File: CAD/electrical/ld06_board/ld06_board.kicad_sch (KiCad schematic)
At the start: 9 parts, among them J1 RS485, J2 LED Strip, J3 Conn_01x04_Pin, J4 I2C, U1 MAX485E, U2 SeeeduinoXIAO

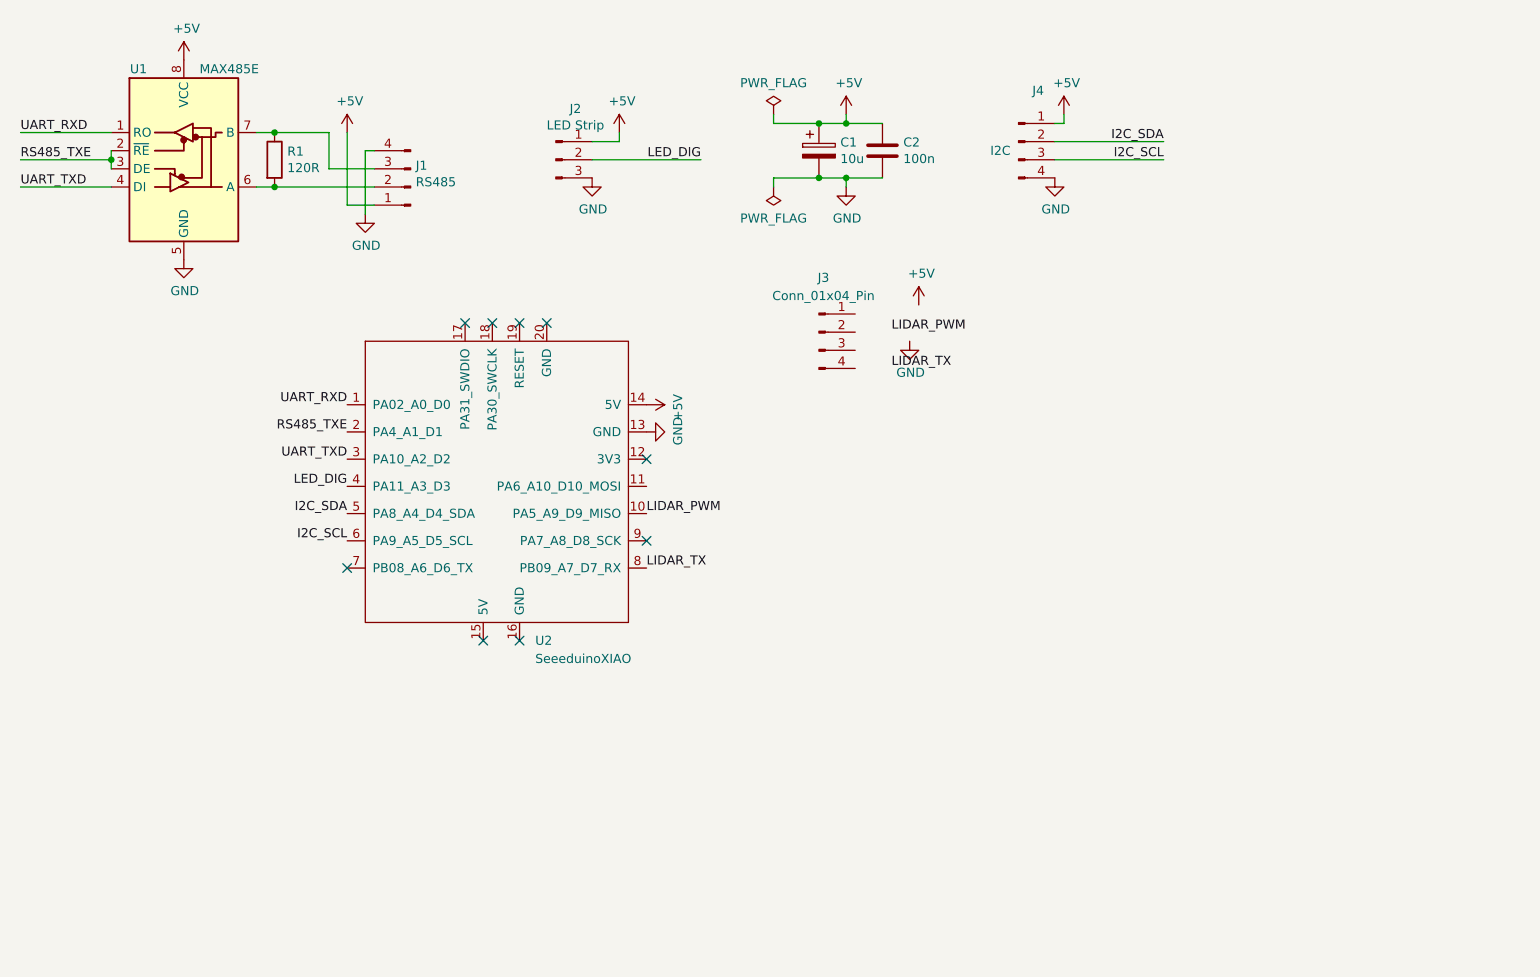
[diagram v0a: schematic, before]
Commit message: sync LD06 board
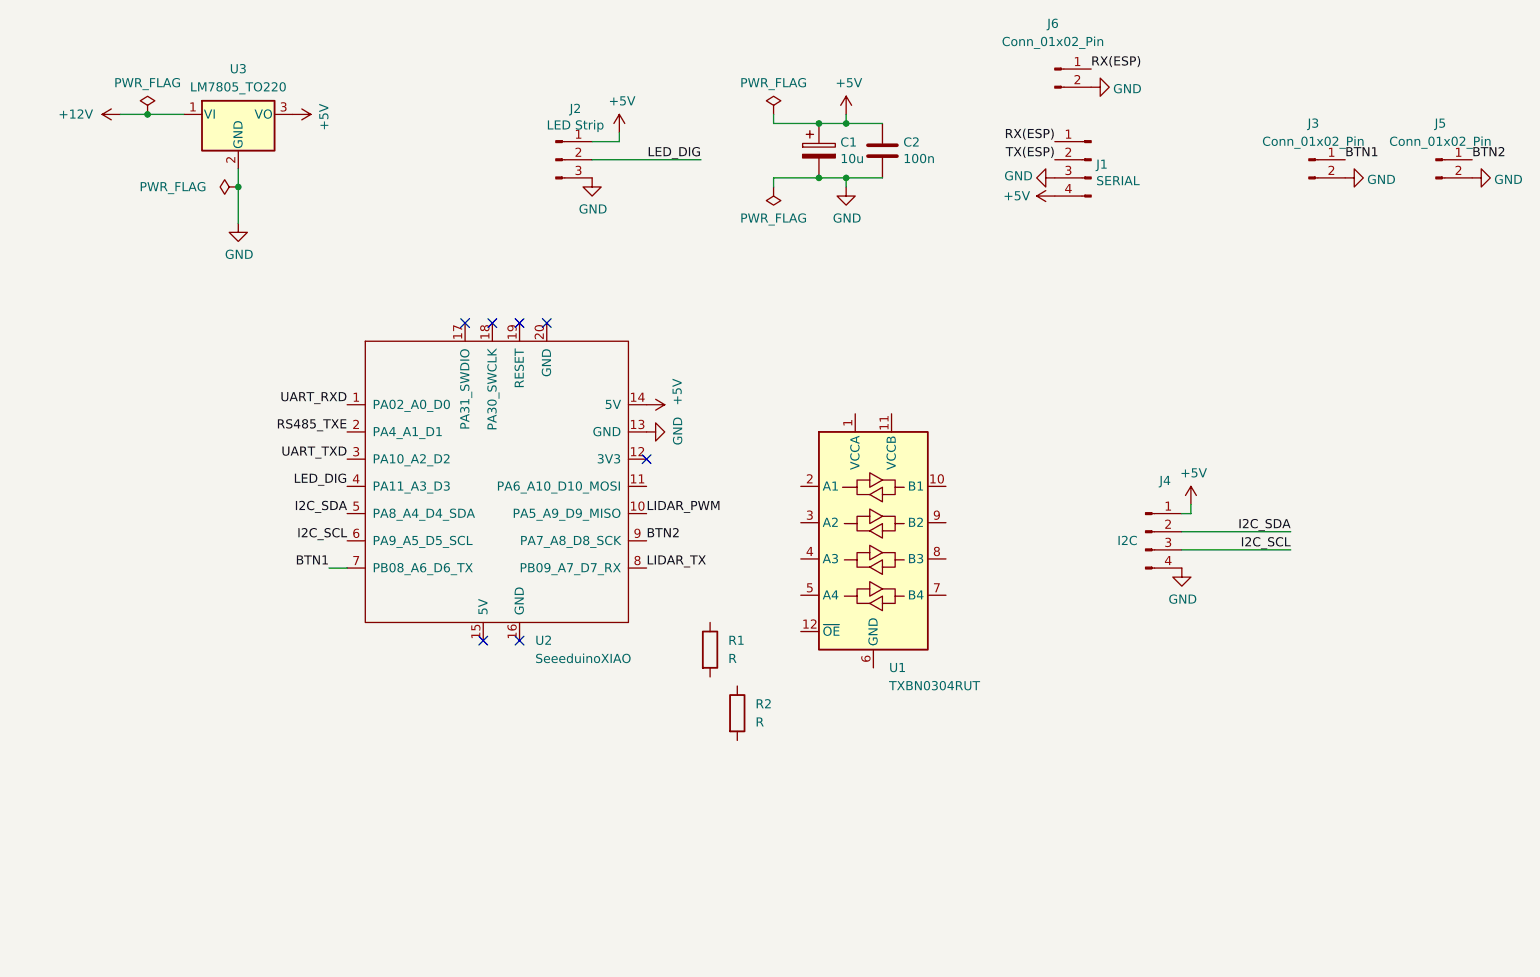
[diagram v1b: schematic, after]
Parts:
- removed J3: Conn_01x04_Pin, Connector_Molex:Molex_KK-254_AE-6410-04A_1x04_P2.54mm_Vertical, symbol Connector:Conn_01x04_Pin
- removed U1: MAX485E, Package_SO:SOIC-8_3.9x4.9mm_P1.27mm, symbol Interface_UART:MAX485E
- added J3, J5, J6: Conn_01x02_Pin, Connector_Molex:Molex_KK-254_AE-6410-02A_1x02_P2.54mm_Vertical, symbol Connector:Conn_01x02_Pin
- added R2: R, Resistor_THT:R_Axial_DIN0309_L9.0mm_D3.2mm_P12.70mm_Horizontal, symbol Device:R
- added U1: TXBN0304RUT, Package_DIP:DIP-12_W10.16mm, symbol Logic_LevelTranslator:TXBN0304RUT
- added U3: LM7805_TO220, Package_TO_SOT_THT:TO-220-3_Vertical, symbol Regulator_Linear:LM7805_TO220
- J1: value RS485 -> SERIAL
- R1: value 120R -> R; footprint Resistor_SMD:R_0603_1608Metric -> Resistor_THT:R_Axial_DIN0309_L9.0mm_D3.2mm_P12.70mm_Horizontal
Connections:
- net +5V: now also J1.4 (Pin_4), U3.3 (VO); no longer J1.1 (Pin_1)
- net GND: now also J1.3 (Pin_3), J3.2 (Pin_2), J5.2 (Pin_2), J6.2 (Pin_2), U3.2 (GND); no longer J1.4 (Pin_4)
- net at R1.2: no longer J1.2 (Pin_2)
- net at R1.1: no longer J1.3 (Pin_3)
- net BTN1: now reaches U2.7 (PB08_A6_D6_TX)
- net BTN1: now also J3.1 (Pin_1)
- net BTN2: now reaches U2.9 (PA7_A8_D8_SCK)
- net BTN2: now also J5.1 (Pin_1)
- new net +12V: U3.1 (VI)
- new net RX(ESP): J1.1 (Pin_1), J6.1 (Pin_1)
- new net TX(ESP): J1.2 (Pin_2)
- no-connect marks 9 -> 7
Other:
- moved on the sheet: J4

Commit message: update PCB
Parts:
- added J7: I2C, Connector_Molex:Molex_KK-254_AE-6410-04A_1x04_P2.54mm_Vertical, symbol Connector:Conn_01x04_Male
- added J9: Battery in, Connector_BarrelJack:BarrelJack_Horizontal, symbol main_board-rescue:Conn_01x02_Male-Connector
- C2: footprint Capacitor_SMD:C_0603_1608Metric -> Resistor_THT:R_Axial_DIN0204_L3.6mm_D1.6mm_P5.08mm_Vertical
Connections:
- net +12V: now also J9.1 (Pin_1)
- net +5V: now also J7.1 (Pin_1)
- net GND: now also J7.4 (Pin_4), J9.2 (Pin_2)
- net I2C_SCL: now also J7.3 (Pin_3)
- net I2C_SDA: now also J7.2 (Pin_2)

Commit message: update
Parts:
- removed U2: SeeeduinoXIAO, Seeeduino XIAO KICAD:XIAO-ESP32-C3-DIP, symbol Seeeduino XIAO:SeeeduinoXIAO
- added U2: ESP32-C3_SUPERMINI_TH, ESP32-C3_SUPERMINI_TH:MODULE_ESP32-C3_SUPERMINI, symbol ESP32-C3_SUPERMINI_TH:ESP32-C3_SUPERMINI_TH
- U1: footprint Package_DIP:DIP-12_W10.16mm -> (none)
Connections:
- net +5V: now also U1.1 (VCCA), U2.5V
- net BTN1: now also U2.5 (GPIO5)
- net BTN2: now also U2.7 (GPIO7)
- net GND: now also U1.12 (~{OE}), U1.6 (GND), U2.G (GND)
- net I2C_SCL: now also U1.2 (A1)
- net I2C_SDA: now also U1.3 (A2)
- net LED_DIG: now also U2.1 (GPIO1)
- net RX(ESP): now also U2.20 (GPIO20)
- net TX(ESP): now also U2.21 (GPIO21)
- net 3V3_SCL: now reaches R2.1
- net 3V3_SCL: now also U1.10 (B1), U2.4 (GPIO4)
- net +3V3: now reaches R2.2
- net +3V3: now also R1.2, U1.11 (VCCB), U2.3.3 (3V3)
- net 3V3_SDA: now reaches R1.1
- net 3V3_SDA: now also U1.9 (B2), U2.3 (GPIO3)
- no-connect marks 7 -> 10
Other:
- moved on the sheet: U1

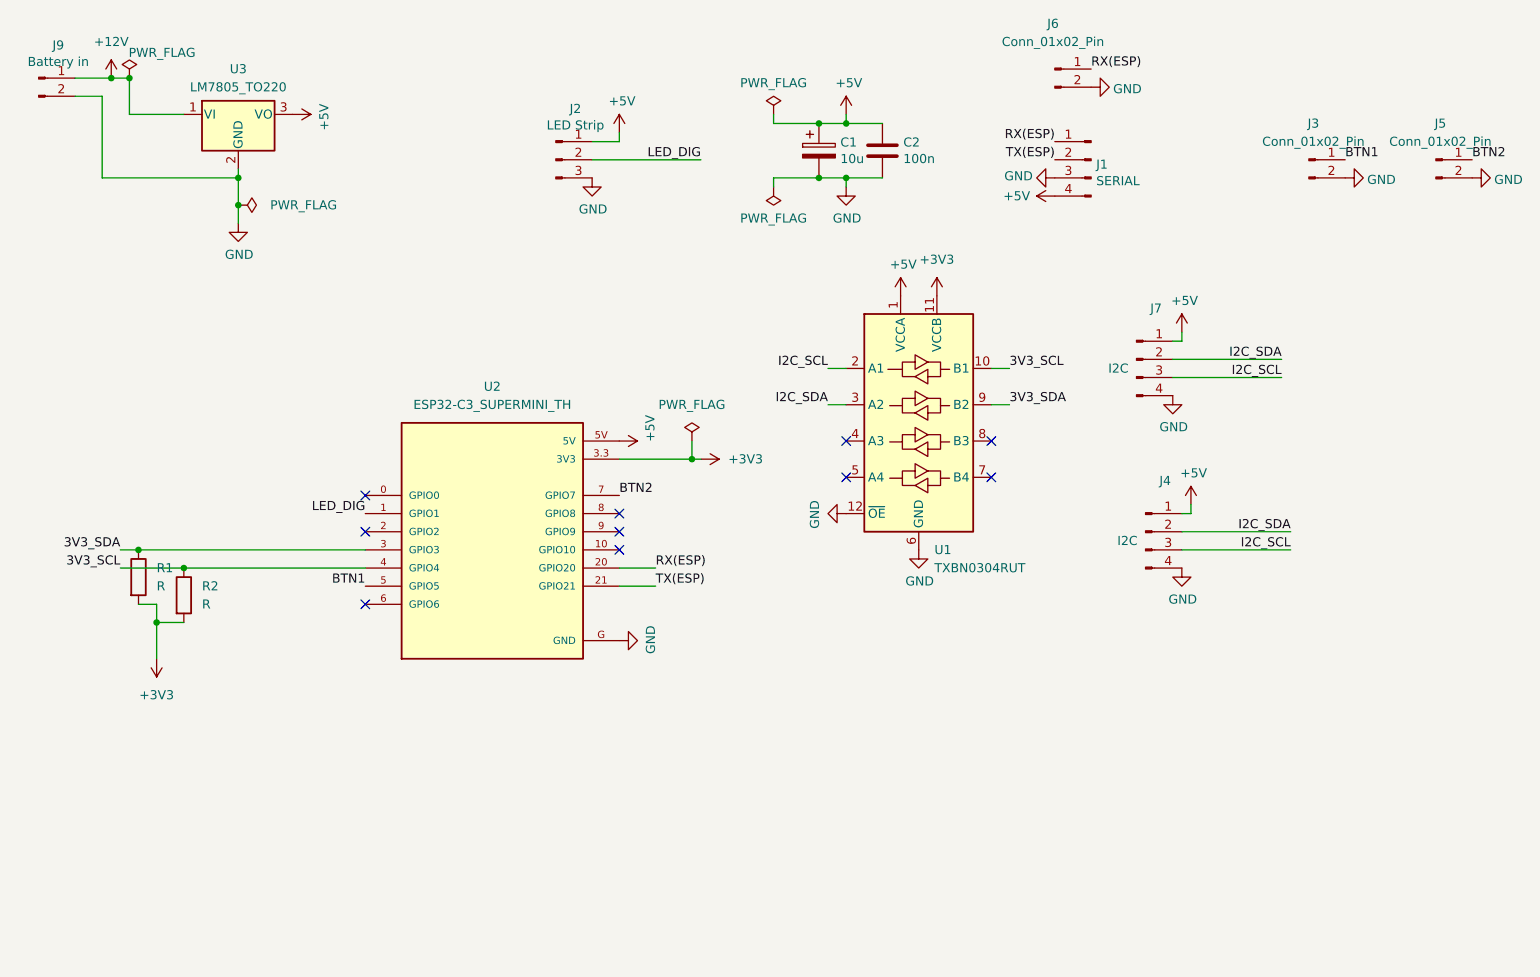
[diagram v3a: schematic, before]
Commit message: LD06 board colplet
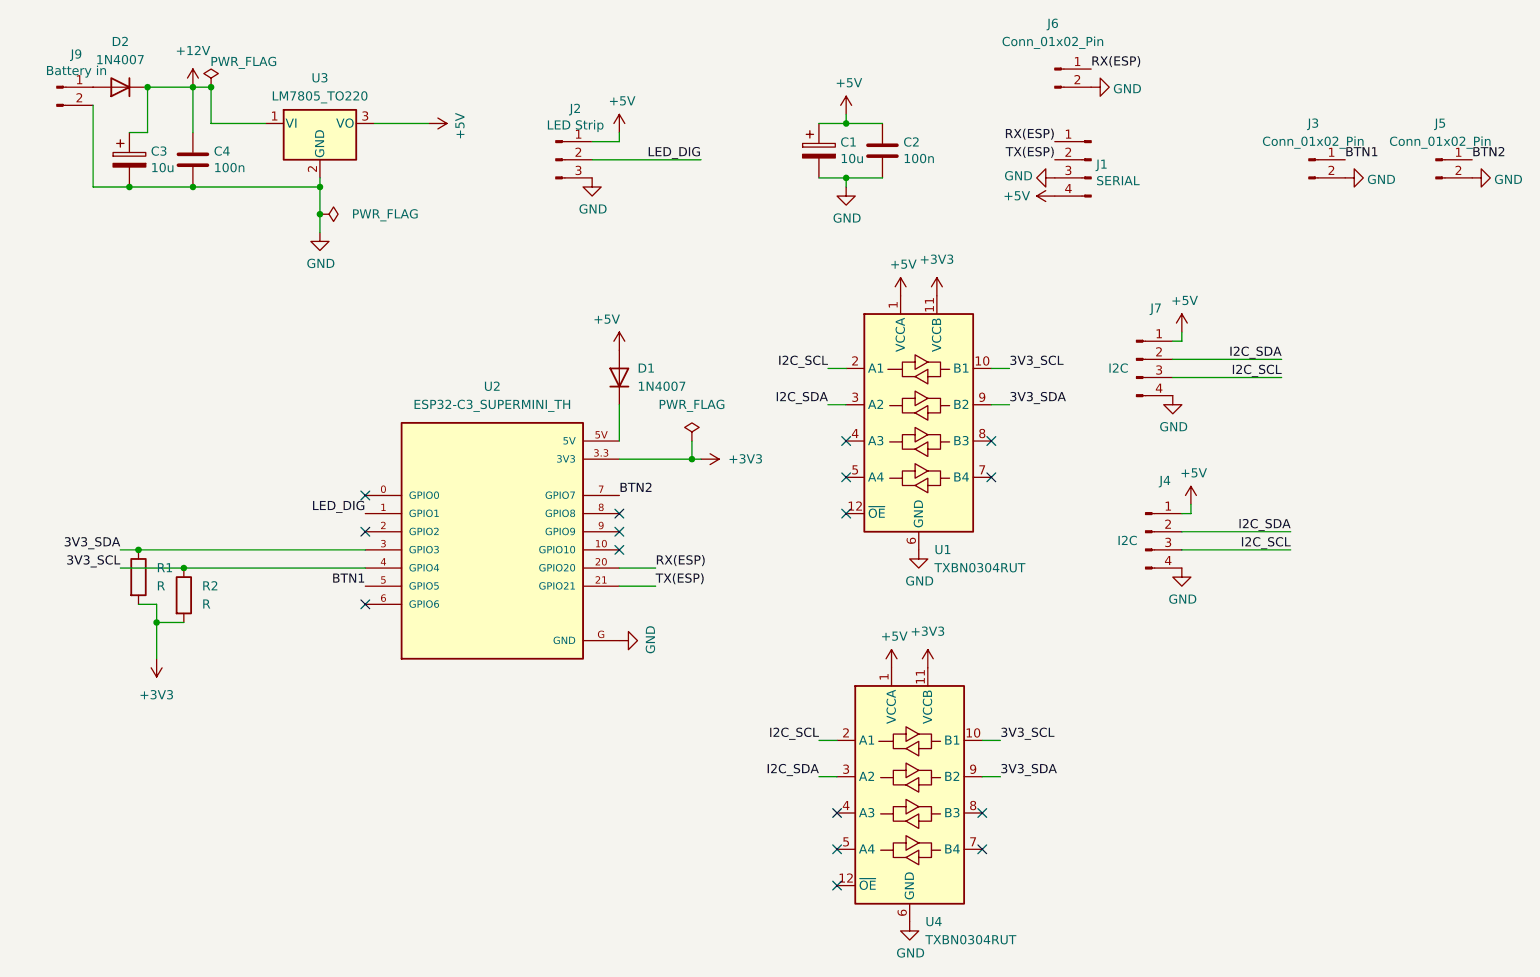
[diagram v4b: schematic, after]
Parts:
- added C3: 10u, Capacitor_THT:CP_Radial_D8.0mm_P3.80mm, symbol ultrasonic_board-rescue:CP-Device
- added C4: 100n, Resistor_THT:R_Axial_DIN0204_L3.6mm_D1.6mm_P5.08mm_Vertical, symbol Device:C
- added D1, D2: 1N4007, Diode_THT:D_T-1_P12.70mm_Horizontal, symbol Device:D
- added U4: TXBN0304RUT, Level_shifter_library:PCA9306_ali, symbol Logic_LevelTranslator:TXBN0304RUT
- U1: footprint (none) -> Level_shifter_library:I2C_ali_level_shifter
- U2: footprint ESP32-C3_SUPERMINI_TH:MODULE_ESP32-C3_SUPERMINI -> ESP32C3MINI:MODULE_ESP32-C3_SUPERMINI
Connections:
- net +12V: now also C3.1, C4.1, D2.1 (K); no longer J9.1 (Pin_1)
- net +3V3: now also U4.11 (VCCB)
- net +5V: now also D1.2 (A), U4.1 (VCCA); no longer U2.5V
- net 3V3_SCL: now also U4.10 (B1)
- net 3V3_SDA: now also U4.9 (B2)
- net GND: now also C3.2, C4.2, U4.6 (GND); no longer U1.12 (~{OE})
- net I2C_SCL: now also U4.2 (A1)
- net I2C_SDA: now also U4.3 (A2)
- new net: D1.1 (K), U2.5V
- new net: D2.2 (A), J9.1 (Pin_1)
- no-connect marks 10 -> 16
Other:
- moved on the sheet: J9, U3
